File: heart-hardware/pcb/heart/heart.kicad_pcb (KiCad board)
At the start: 4 copper layers, 47.6 x 45.2 mm, 66 parts, among them J1 3V0, J2 DIO, J3 CLK, J5 TOUCH_KEY, SW1 SW_SPDT, U1 STM32L031F6Px, U2 TCA6416APWR, U3 LIS3DH, U4 Holtek-Semicon-BS812A-1

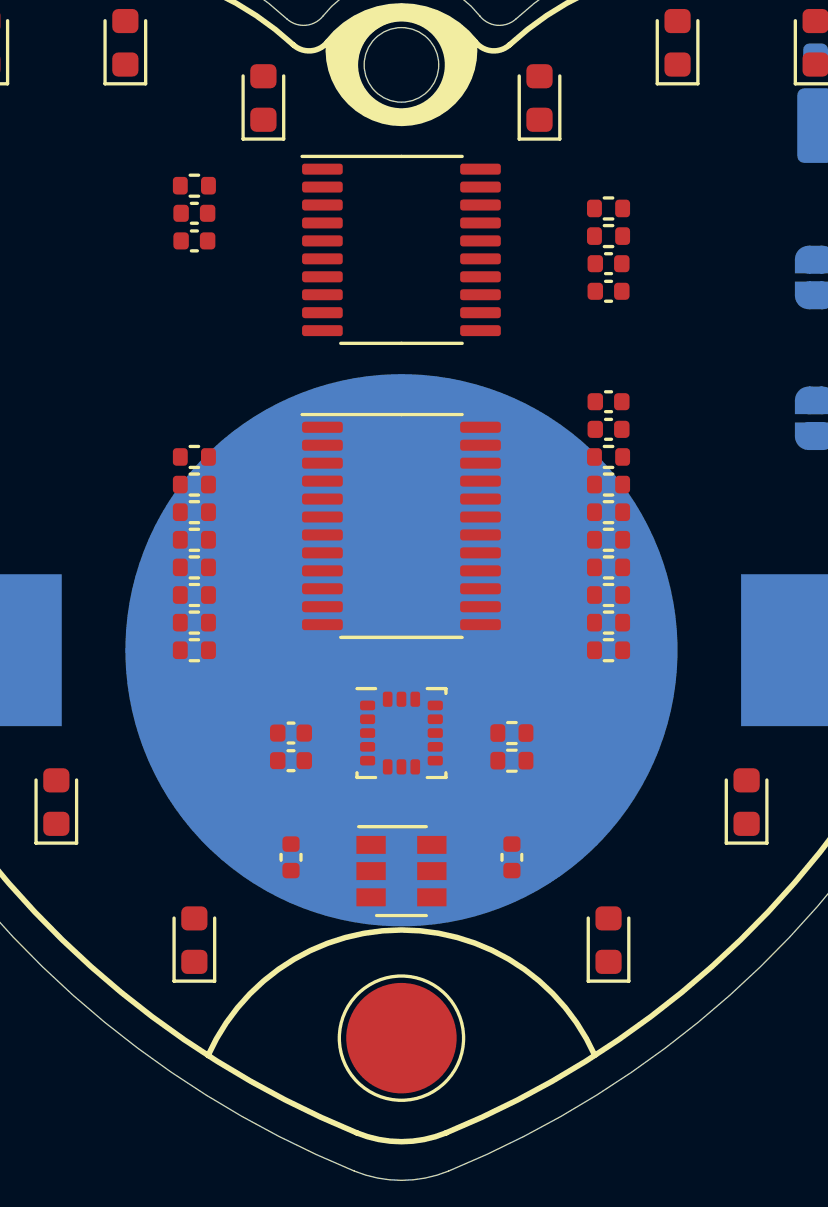
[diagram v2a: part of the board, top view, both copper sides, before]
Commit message: Added jumper to choose interuppt lines
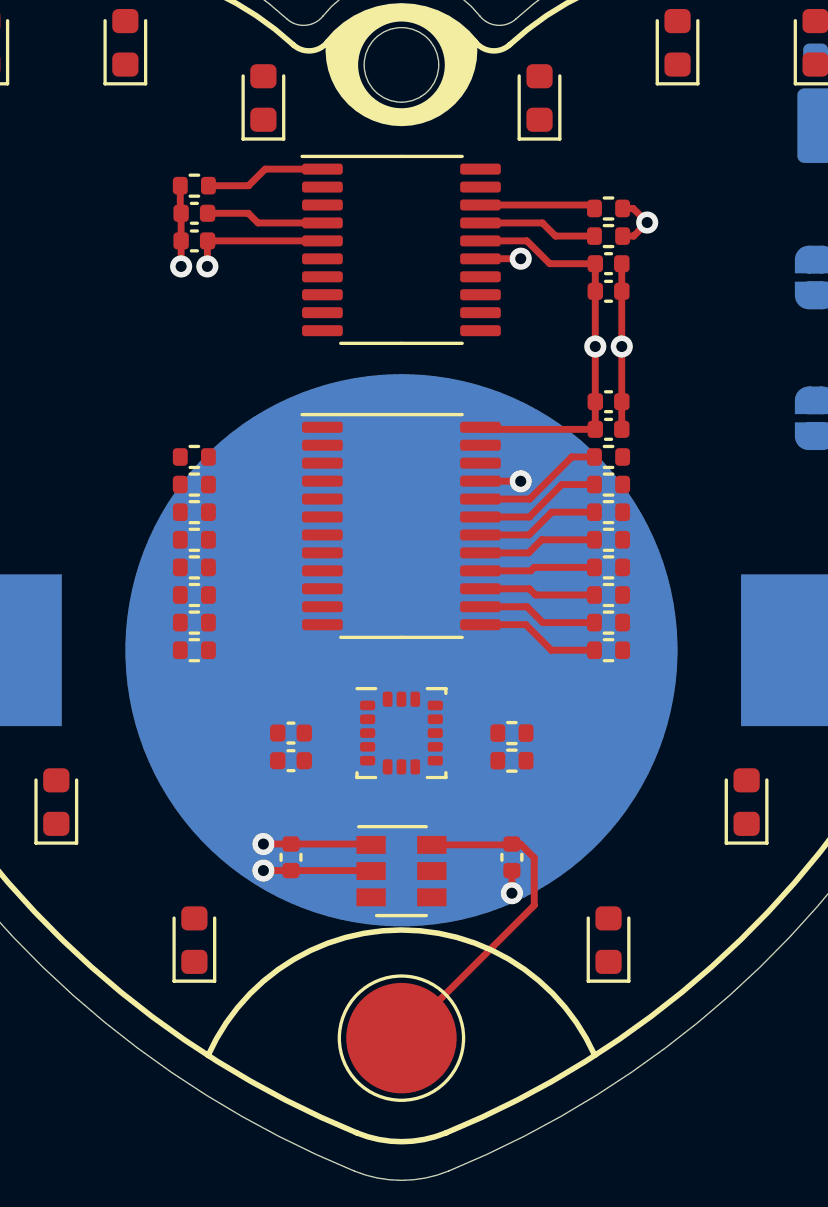
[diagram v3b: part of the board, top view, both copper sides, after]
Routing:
- net +3V0: track 0.00 -> 25.9 mm, vias 0 -> 4
- net GND: track 0.00 -> 16.6 mm, vias 0 -> 6
- net Net-(C10-Pad2): track 0.00 -> 12.5 mm
- net Net-(R15-Pad1): track 0.00 -> 4.76 mm
- net Net-(R14-Pad1): track 0.00 -> 4.61 mm
- net Net-(R8-Pad1): track 0.00 -> 4.51 mm
- net Net-(R13-Pad1): track 0.00 -> 4.47 mm
- net Net-(R21-Pad2): track 0.00 -> 4.38 mm
- net Net-(R9-Pad1): track 0.00 -> 4.37 mm
- net Net-(R12-Pad1): track 0.00 -> 4.32 mm
- net I2C_SCL: track 0.00 -> 4.32 mm
- net Net-(C5-Pad1): track 0.00 -> 4.30 mm
- net Net-(R10-Pad1): track 0.00 -> 4.22 mm
- net Net-(R11-Pad1): track 0.00 -> 4.18 mm
- net I2C_SDA: track 0.00 -> 4.18 mm
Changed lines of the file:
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@@
     (thickness 1.6)
     (drawings 42)
-    (tracks 0)
+    (tracks 90)
     (zones 0)
     (modules 66)
@@
     (effects (font (size 2.900172 2.610154) (thickness 0.362521)) (justify left top))
   )
+  (via (at 54.32 75.88) (size 0.8) (drill 0.4) (layers F.Cu B.Cu) (net 2))
+  (via (at 42.02 68.1) (size 0.8) (drill 0.4) (layers F.Cu B.Cu) (net 2))
+  (via (at 42.97 68.1) (size 0.8) (drill 0.4) (layers F.Cu B.Cu) (net 3))
+  (via (at 54.32 67.82) (size 0.8) (drill 0.4) (layers F.Cu B.Cu) (net 2))
+  (via (at 57.02 71) (size 0.8) (drill 0.4) (layers F.Cu B.Cu) (net 3))
+  (via (at 57.98 71) (size 0.8) (drill 0.4) (layers F.Cu B.Cu) (net 2))
+  (segment (start 52.8675 67.82) (end 52.8625 67.825) (width 0.25) (layer F.Cu) (net 2))
+  (segment (start 54.32 67.82) (end 52.8675 67.82) (width 0.25) (layer F.Cu) (net 2))
+  (segment (start 42.02 68.1) (end 42.02 67.175) (width 0.25) (layer F.Cu) (net 2))
+  (segment (start 57.98 71) (end 57.98 73) (width 0.25) (layer F.Cu) (net 2))
+  (segment (start 57.98 71) (end 57.98 69) (width 0.25) (layer F.Cu) (net 2))
+  (segment (start 57.98 69) (end 57.98 68) (width 0.25) (layer F.Cu) (net 2))
+  (segment (start 57.98 73) (end 57.98 74) (width 0.25) (layer F.Cu) (net 2))
+  (segment (start 42.02 67.175) (end 42.02 66.175) (width 0.25) (layer F.Cu) (net 2))
+  (segment (start 41.99 66.145) (end 42.02 66.175) (width 0.25) (layer F.Cu) (net 2))
+  (segment (start 41.99 65.175) (end 41.99 66.145) (width 0.25) (layer F.Cu) (net 2))
+  (segment (start 52.8675 75.88) (end 52.8625 75.875) (width 0.25) (layer F.Cu) (net 2))
+  (segment (start 54.32 75.88) (end 52.8675 75.88) (width 0.25) (layer F.Cu) (net 2))
+  (segment (start 48.88 89.98) (end 48.9 90) (width 0.25) (layer F.Cu) (net 2))
+  (segment (start 46 89.98) (end 48.88 89.98) (width 0.25) (layer F.Cu) (net 2))
+  (segment (start 46 89.98) (end 45 89.98) (width 0.25) (layer F.Cu) (net 2))
+  (segment (start 45 89.98) (end 45 89.98) (width 0.25) (layer F.Cu) (net 2))
+  (via (at 45 89.98) (size 0.8) (drill 0.4) (layers F.Cu B.Cu) (net 2))
+  (segment (start 54 89.98) (end 54 90.8) (width 0.25) (layer F.Cu) (net 2))
+  (segment (start 54 90.8) (end 54 90.8) (width 0.25) (layer F.Cu) (net 2))
+  (via (at 54 90.8) (size 0.8) (drill 0.4) (layers F.Cu B.Cu) (net 2))
+  (via (at 58.9 66.51) (size 0.8) (drill 0.4) (layers F.Cu B.Cu) (net 3))
+  (segment (start 57.02 69) (end 57.02 68) (width 0.25) (layer F.Cu) (net 3))
+  (segment (start 58.39 66) (end 58.9 66.51) (width 0.25) (layer F.Cu) (net 3))
+  (segment (start 58.01 66) (end 58.39 66) (width 0.25) (layer F.Cu) (net 3))
+  (segment (start 58.41 67) (end 58.9 66.51) (width 0.25) (layer F.Cu) (net 3))
+  (segment (start 58.01 67) (end 58.41 67) (width 0.25) (layer F.Cu) (net 3))
+  (segment (start 57.02 68) (end 55.37 68) (width 0.25) (layer F.Cu) (net 3))
+  (segment (start 54.545 67.175) (end 52.8625 67.175) (width 0.25) (layer F.Cu) (net 3))
+  (segment (start 55.37 68) (end 54.545 67.175) (width 0.25) (layer F.Cu) (net 3))
+  (segment (start 42.97 67.185) (end 42.98 67.175) (width 0.25) (layer F.Cu) (net 3))
+  (segment (start 42.97 68.1) (end 42.97 67.185) (width 0.25) (layer F.Cu) (net 3))
+  (segment (start 42.98 67.175) (end 47.1375 67.175) (width 0.25) (layer F.Cu) (net 3))
+  (segment (start 57.02 71) (end 57.02 69) (width 0.25) (layer F.Cu) (net 3))
+  (segment (start 57.02 71) (end 57.02 73) (width 0.25) (layer F.Cu) (net 3))
+  (segment (start 57.02 73) (end 57.02 74) (width 0.25) (layer F.Cu) (net 3))
+  (segment (start 52.9375 74) (end 52.8625 73.925) (width 0.25) (layer F.Cu) (net 3))
+  (segment (start 57.02 74) (end 52.9375 74) (width 0.25) (layer F.Cu) (net 3))
+  (segment (start 48.87 89.02) (end 48.9 89.05) (width 0.25) (layer F.Cu) (net 3))
+  (segment (start 46 89.02) (end 48.87 89.02) (width 0.25) (layer F.Cu) (net 3))
+  (segment (start 46 89.02) (end 45 89.02) (width 0.25) (layer F.Cu) (net 3))
+  (segment (start 45 89.02) (end 45 89.02) (width 0.25) (layer F.Cu) (net 3))
+  (via (at 45 89.02) (size 0.8) (drill 0.4) (layers F.Cu B.Cu) (net 3))
+  (segment (start 56.99 67) (end 55.58 67) (width 0.25) (layer F.Cu) (net 24))
+  (segment (start 55.105 66.525) (end 52.8625 66.525) (width 0.25) (layer F.Cu) (net 24))
+  (segment (start 55.58 67) (end 55.105 66.525) (width 0.25) (layer F.Cu) (net 24))
+  (segment (start 56.99 66) (end 56.98 66) (width 0.25) (layer F.Cu) (net 25))
+  (segment (start 56.855 65.875) (end 52.8625 65.875) (width 0.25) (layer F.Cu) (net 25))
+  (segment (start 56.98 66) (end 56.855 65.875) (width 0.25) (layer F.Cu) (net 25))
+  (segment (start 42.98 66.175) (end 44.455 66.175) (width 0.25) (layer F.Cu) (net 43))
+  (segment (start 44.805 66.525) (end 47.1375 66.525) (width 0.25) (layer F.Cu) (net 43))
+  (segment (start 44.455 66.175) (end 44.805 66.525) (width 0.25) (layer F.Cu) (net 43))
+  (segment (start 53.97 89.05) (end 54 89.02) (width 0.25) (layer F.Cu) (net 45))
+  (segment (start 51.1 89.05) (end 53.97 89.05) (width 0.25) (layer F.Cu) (net 45))
+  (segment (start 54.31 89.02) (end 54.81 89.52) (width 0.25) (layer F.Cu) (net 45))
+  (segment (start 54 89.02) (end 54.31 89.02) (width 0.25) (layer F.Cu) (net 45))
+  (segment (start 54.81 91.24) (end 50 96.05) (width 0.25) (layer F.Cu) (net 45))
+  (segment (start 54.81 89.52) (end 54.81 91.24) (width 0.25) (layer F.Cu) (net 45))
+  (segment (start 52.8625 81.075) (end 54.505 81.075) (width 0.25) (layer F.Cu) (net 57))
+  (segment (start 55.43 82) (end 56.99 82) (width 0.25) (layer F.Cu) (net 57))
+  (segment (start 54.505 81.075) (end 55.43 82) (width 0.25) (layer F.Cu) (net 57))
+  (segment (start 52.8625 80.425) (end 54.545 80.425) (width 0.25) (layer F.Cu) (net 58))
+  (segment (start 55.12 81) (end 56.99 81) (width 0.25) (layer F.Cu) (net 58))
+  (segment (start 54.545 80.425) (end 55.12 81) (width 0.25) (layer F.Cu) (net 58))
+  (segment (start 52.8625 79.775) (end 54.635 79.775) (width 0.25) (layer F.Cu) (net 59))
+  (segment (start 54.86 80) (end 56.99 80) (width 0.25) (layer F.Cu) (net 59))
+  (segment (start 54.635 79.775) (end 54.86 80) (width 0.25) (layer F.Cu) (net 59))
+  (segment (start 52.8625 79.125) (end 54.685 79.125) (width 0.25) (layer F.Cu) (net 60))
+  (segment (start 54.81 79) (end 56.99 79) (width 0.25) (layer F.Cu) (net 60))
+  (segment (start 54.685 79.125) (end 54.81 79) (width 0.25) (layer F.Cu) (net 60))
+  (segment (start 52.8625 78.475) (end 54.60423 78.475) (width 0.25) (layer F.Cu) (net 61))
+  (segment (start 55.07923 78) (end 56.99 78) (width 0.25) (layer F.Cu) (net 61))
+  (segment (start 54.60423 78.475) (end 55.07923 78) (width 0.25) (layer F.Cu) (net 61))
+  (segment (start 52.8625 77.825) (end 54.61782 77.825) (width 0.25) (layer F.Cu) (net 62))
+  (segment (start 55.44282 77) (end 56.99 77) (width 0.25) (layer F.Cu) (net 62))
+  (segment (start 54.61782 77.825) (end 55.44282 77) (width 0.25) (layer F.Cu) (net 62))
+  (segment (start 52.8625 77.175) (end 54.63141 77.175) (width 0.25) (layer F.Cu) (net 63))
+  (segment (start 55.80641 76) (end 56.99 76) (width 0.25) (layer F.Cu) (net 63))
+  (segment (start 54.63141 77.175) (end 55.80641 76) (width 0.25) (layer F.Cu) (net 63))
+  (segment (start 52.8625 76.525) (end 54.645 76.525) (width 0.25) (layer F.Cu) (net 64))
+  (segment (start 56.17 75) (end 56.99 75) (width 0.25) (layer F.Cu) (net 64))
+  (segment (start 54.645 76.525) (end 56.17 75) (width 0.25) (layer F.Cu) (net 64))
+  (segment (start 43.01 65.175) (end 44.465 65.175) (width 0.25) (layer F.Cu) (net 65))
+  (segment (start 45.065 64.575) (end 47.1375 64.575) (width 0.25) (layer F.Cu) (net 65))
+  (segment (start 44.465 65.175) (end 45.065 64.575) (width 0.25) (layer F.Cu) (net 65))
 )

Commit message: Routing in progress
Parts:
- added PA1: SolderJumper_3_Open, Jumper:SolderJumper-3_P1.3mm_Open_RoundedPad1.0x1.5mm_NumberLabels, B.Cu at (33.1, 63.0)
- added PA2: SolderJumper_3_Open, Jumper:SolderJumper-3_P1.3mm_Open_RoundedPad1.0x1.5mm_NumberLabels, B.Cu at (35.6, 63.0)
- CR2450: value BT1 -> CR2450
- moved JP3 3.56 mm to (32.8, 76.1)
- moved R24 3.56 mm to (33.0, 78.0)
- moved J1 3.56 mm to (32.2, 67.8)
- moved J2 3.56 mm to (32.2, 71.8)
- moved J3 3.56 mm to (32.2, 69.8)
- moved J4 3.56 mm to (32.2, 73.8)
- renumbered Je to J4, R4 to R0
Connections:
- U1 pad 7: Net-(U1-Pad7) -> PA1
- U1 pad 8: LIS3DH_INT2 -> PA2
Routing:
- net +3V0: track 25.9 -> 46.9 mm, vias 4 -> 20
- net Net-(R7-Pad1): track 0.00 -> 4.78 mm
- net Net-(R6-Pad1): track 0.00 -> 4.63 mm
- net Net-(R5-Pad1): track 0.00 -> 4.49 mm
- net Net-(R0-Pad1): track 0.00 -> 4.49 mm
- net Net-(R4-Pad1): track 0.00 -> 4.34 mm
- net Net-(R1-Pad1): track 0.00 -> 4.34 mm
- net Net-(R3-Pad1): track 0.00 -> 4.20 mm
- net Net-(R2-Pad1): track 0.00 -> 4.20 mm
- net GND: track 16.6 -> 18.6 mm, vias 6 -> 7
- net Net-(D9-Pad1): track 0.00 -> 1.21 mm, vias 0 -> 1
- net Net-(D8-Pad1): track 0.00 -> 1.21 mm, vias 0 -> 1
- net Net-(D7-Pad1): track 0.00 -> 1.21 mm, vias 0 -> 1
- net Net-(D6-Pad1): track 0.00 -> 1.21 mm, vias 0 -> 1
- net Net-(D5-Pad1): track 0.00 -> 1.21 mm, vias 0 -> 1
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
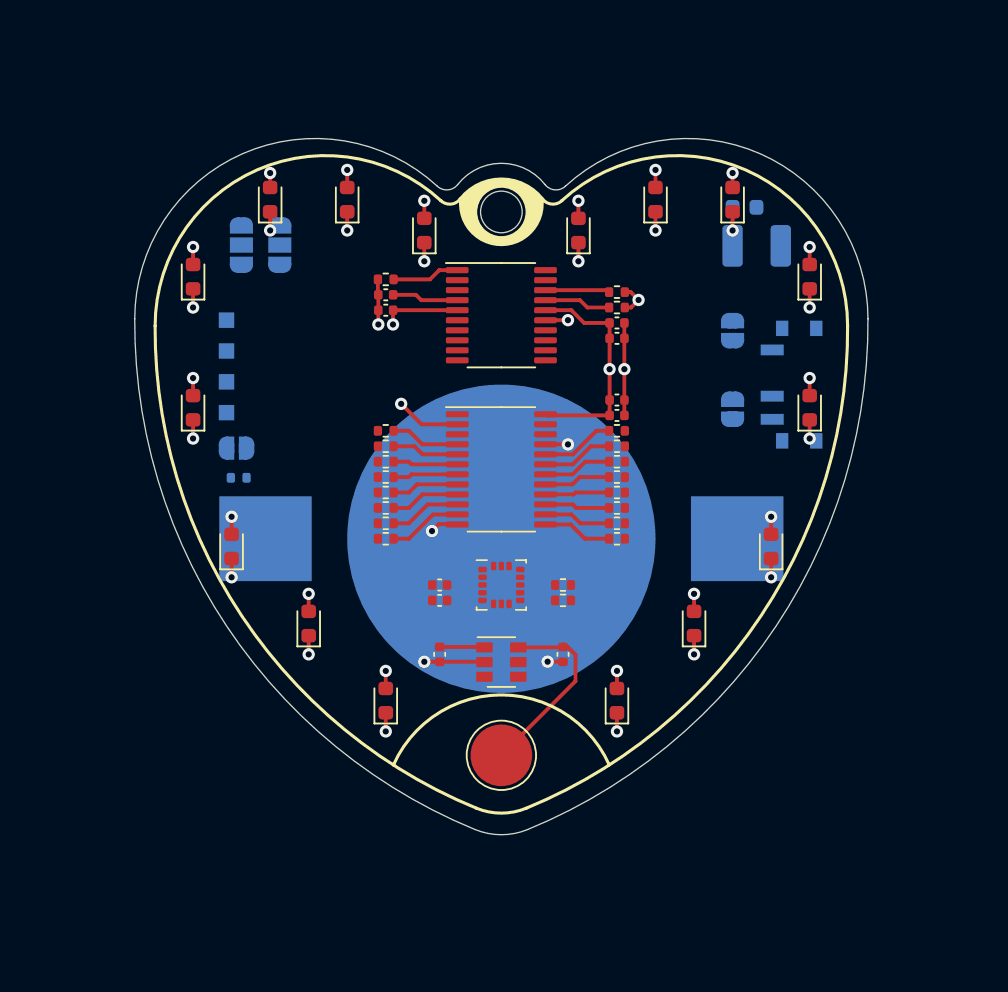
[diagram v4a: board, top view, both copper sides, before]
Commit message: Some trace routed, backup with vias on leds to trace route in inner layer
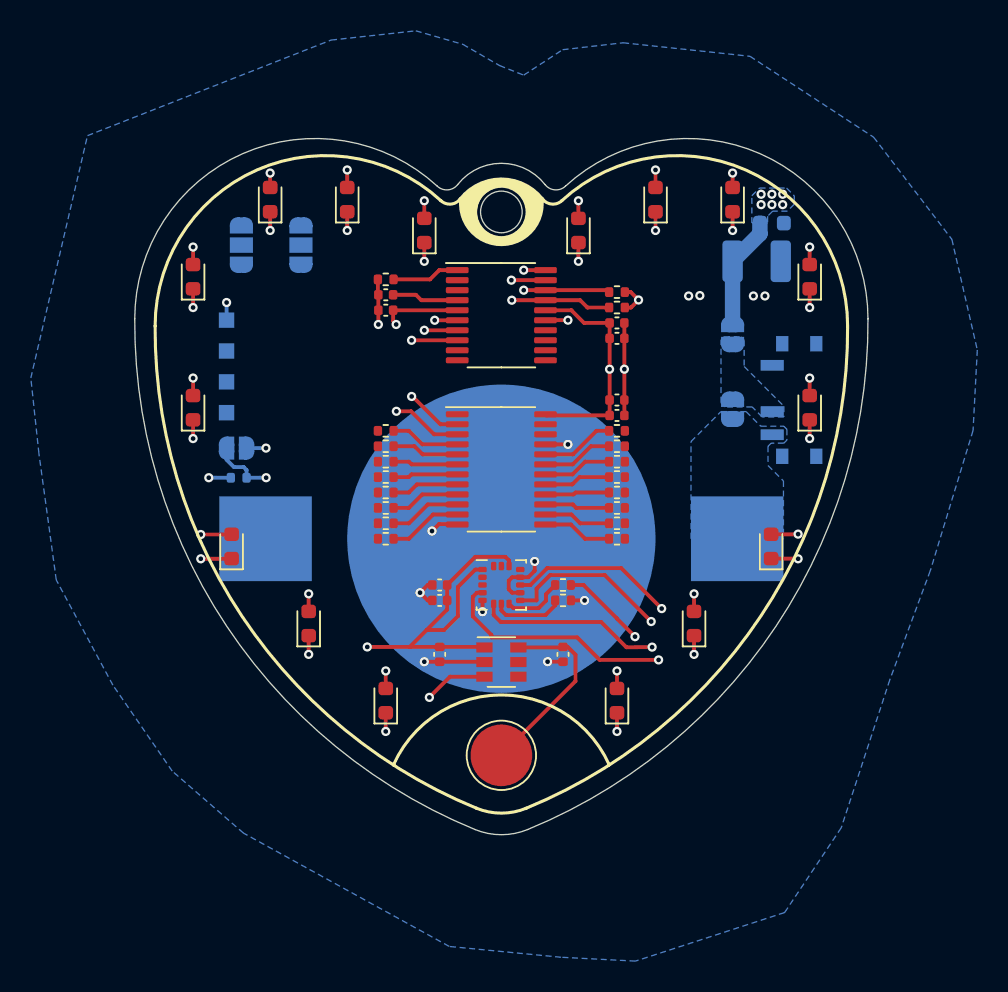
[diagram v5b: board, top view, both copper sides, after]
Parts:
- moved C1 2.05 mm to (67.5, 61.5)
- moved PA2 1.38 mm to (37.0, 63.0)
- moved C0 1.00 mm to (66.6, 64.0)
- moved SW1 1.00 mm to (69.0, 73.0)
- moved JP2 0.25 mm to (65.0, 68.8)
- turned JP3 to 180 degrees
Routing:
- net +3V0: track 46.9 -> 84.7 mm, vias 20 -> 30
- net I2C_SCL: track 4.32 -> 21.8 mm, vias 0 -> 2
- net I2C_SDA: track 4.18 -> 17.5 mm, vias 0 -> 2
- net GND: track 18.6 -> 31.1 mm, vias 7 -> 15
- net LIS3DH_INT1: track 0.00 -> 12.2 mm, vias 0 -> 2
- net LIS3DH_INT2: track 0.00 -> 10.9 mm, vias 0 -> 1
- net TCA6416A_RESET: track 0.00 -> 8.67 mm, vias 0 -> 2
- net Net-(R26-Pad2): track 0.00 -> 4.62 mm
- net TOUCH_KEY_1: track 0.00 -> 4.13 mm, vias 0 -> 1
- net Net-(R25-Pad1): track 0.00 -> 4.01 mm
- net PA2: track 0.00 -> 2.96 mm, vias 0 -> 1
- net SWDIO: track 0.00 -> 2.21 mm, vias 0 -> 1
- net PA1: track 0.00 -> 2.14 mm, vias 0 -> 1
- net SWDCLK: track 0.00 -> 1.41 mm, vias 0 -> 1
- net Net-(JP3-Pad1): track 0.00 -> 1.26 mm, vias 0 -> 1
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- added copper zone on B.Cu, net +3V0
- added copper zone on In2.Cu, net +3V0
- added copper zone on B.Cu, net GND
- added copper zone on B.Cu, net Net-(JP1-Pad2)
- added copper zone on B.Cu, net VCC

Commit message: Route completed
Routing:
- net LIS3DH_INT2: track 10.9 -> 59.1 mm, vias 1 -> 2
- net TOUCH_KEY_1: track 4.13 -> 46.2 mm, vias 1 -> 2
- net I2C_SCL: track 21.8 -> 59.8 mm, vias 2 -> 3
- net I2C_SDA: track 17.5 -> 52.1 mm, vias 2 -> 4
- net LIS3DH_INT1: track 12.2 -> 46.1 mm
- net Net-(JP3-Pad1): track 1.26 -> 28.2 mm, vias 1 -> 2
- net SWDCLK: track 1.41 -> 26.2 mm, vias 1 -> 2
- net SWDIO: track 2.21 -> 24.6 mm, vias 1 -> 2
- net PA1: track 2.14 -> 23.2 mm, vias 1 -> 2
- net Net-(D2-Pad1): track 1.21 -> 19.1 mm, vias 1 -> 0
- net Net-(D13-Pad1): track 1.21 -> 19.1 mm, vias 1 -> 0
- net Net-(D14-Pad1): track 1.21 -> 17.3 mm, vias 1 -> 0
- net Net-(D3-Pad1): track 1.21 -> 17.2 mm, vias 1 -> 0
- net Net-(D12-Pad1): track 1.21 -> 17.2 mm, vias 1 -> 0
- net Net-(D1-Pad1): track 1.21 -> 16.0 mm, vias 1 -> 0
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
